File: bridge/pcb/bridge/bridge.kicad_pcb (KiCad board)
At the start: 2 copper layers, 161 x 81 mm, 18 parts, among them J1 Screw_Terminal_01x06, J2 Screw_Terminal_01x06, J3 Screw_Terminal_01x06, J4 Conn_01x23, Q1 PMOS, Q2 PMOS, Q3 PMOS, Q4 PMOS, Q5 PMOS, SW1 SW_SPST, U1 YAAJ_BluePill, U2 J104D2C12VDC.20S

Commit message: Fixed issues, added DAC
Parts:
- added D2: GREEN, LED_THT:LED_D5.0mm, F.Cu at (97.5, 114.8)
- added D3: GREEN, LED_THT:LED_D5.0mm, F.Cu at (104.5, 114.8)
- added D4: GREEN, LED_THT:LED_D5.0mm, F.Cu at (118.5, 114.8)
- added D5: GREEN, LED_THT:LED_D5.0mm, F.Cu at (111.5, 114.8)
- added R10: 1k5, Resistor_THT:R_Axial_DIN0309_L9.0mm_D3.2mm_P12.70mm_Horizontal, F.Cu at (117.8, 63.2)
- added R6: 24k, Resistor_THT:R_Axial_DIN0309_L9.0mm_D3.2mm_P12.70mm_Horizontal, F.Cu at (98.8, 89.8)
- added R7: 24k, Resistor_THT:R_Axial_DIN0309_L9.0mm_D3.2mm_P12.70mm_Horizontal, F.Cu at (104.2, 89.9)
- added R8: 10k, Resistor_THT:R_Axial_DIN0309_L9.0mm_D3.2mm_P12.70mm_Horizontal, F.Cu at (116.5, 89.9)
- added R9: 144k, Resistor_THT:R_Axial_DIN0309_L9.0mm_D3.2mm_P12.70mm_Horizontal, F.Cu at (109.8, 89.9)
- added U3: AD557JN, bridge:AD557JN, F.Cu at (100.0, 65.2)
- Q1, Q2, Q3, Q4, Q5: footprint Package_TO_SOT_THT:TO-3P-3_Horizontal_TabDown -> Package_TO_SOT_THT:TO-220-3_Horizontal_TabDown
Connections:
- U1 pad 25: unconnected-(U1-PA0-Pad25) -> Net-(U1-PA0)
- U1 pad 26: unconnected-(U1-PA1-Pad26) -> Net-(U1-PA1)
- U1 pad 27: unconnected-(U1-PA2-Pad27) -> Net-(U1-PA2)
- U1 pad 28: unconnected-(U1-PA3-Pad28) -> Net-(U1-PA3)
- U1 pad 29: unconnected-(U1-PA4-Pad29) -> Net-(U1-PA4)
- U1 pad 30: unconnected-(U1-PA5-Pad30) -> Net-(U1-PA5)
- U1 pad 31: unconnected-(U1-PA6-Pad31) -> Net-(U1-PA6)
- U1 pad 32: unconnected-(U1-PA7-Pad32) -> Net-(U1-PA7)
- U2 pad 4: ACCEL_AUX_AUTO -> unconnected-(U2-Pad4)
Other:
- board size 161 x 81 mm -> 163 x 83 mm

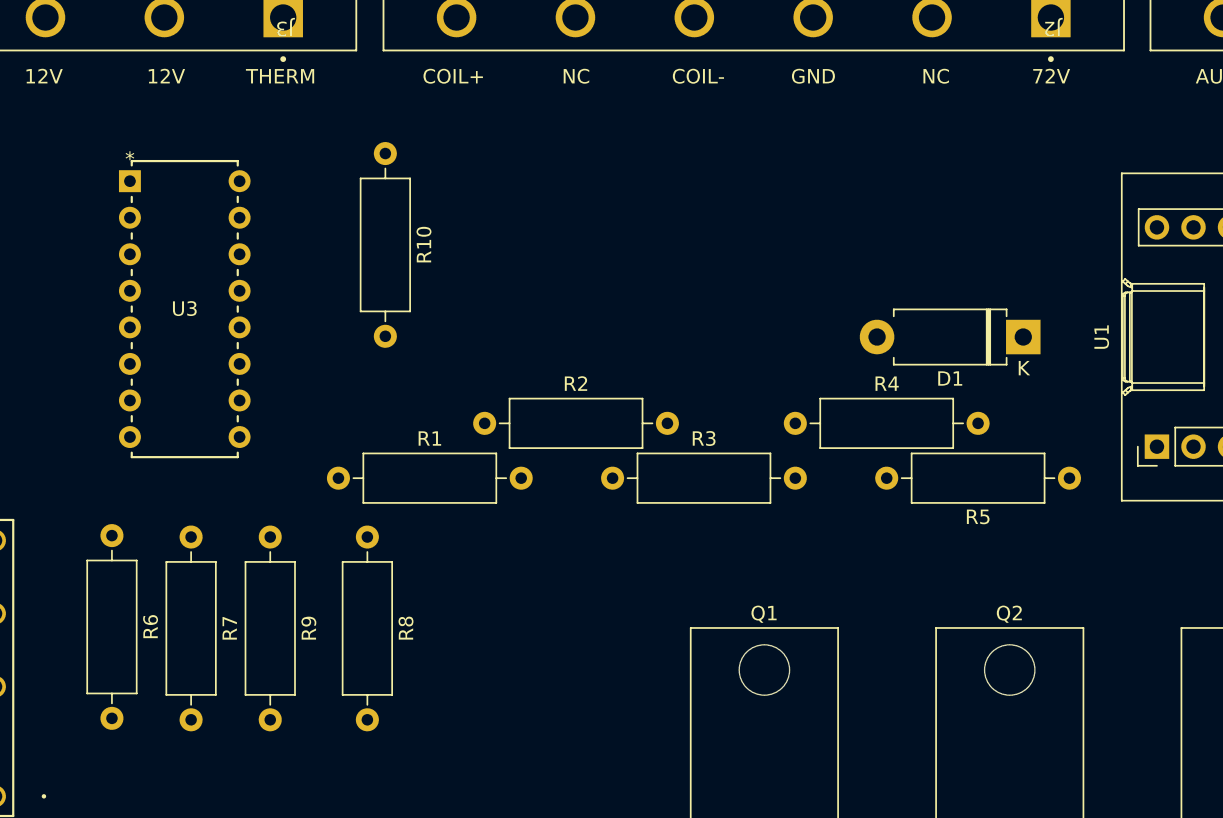
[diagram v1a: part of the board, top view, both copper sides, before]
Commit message: Changed PCB to use correct tht resistor footprint
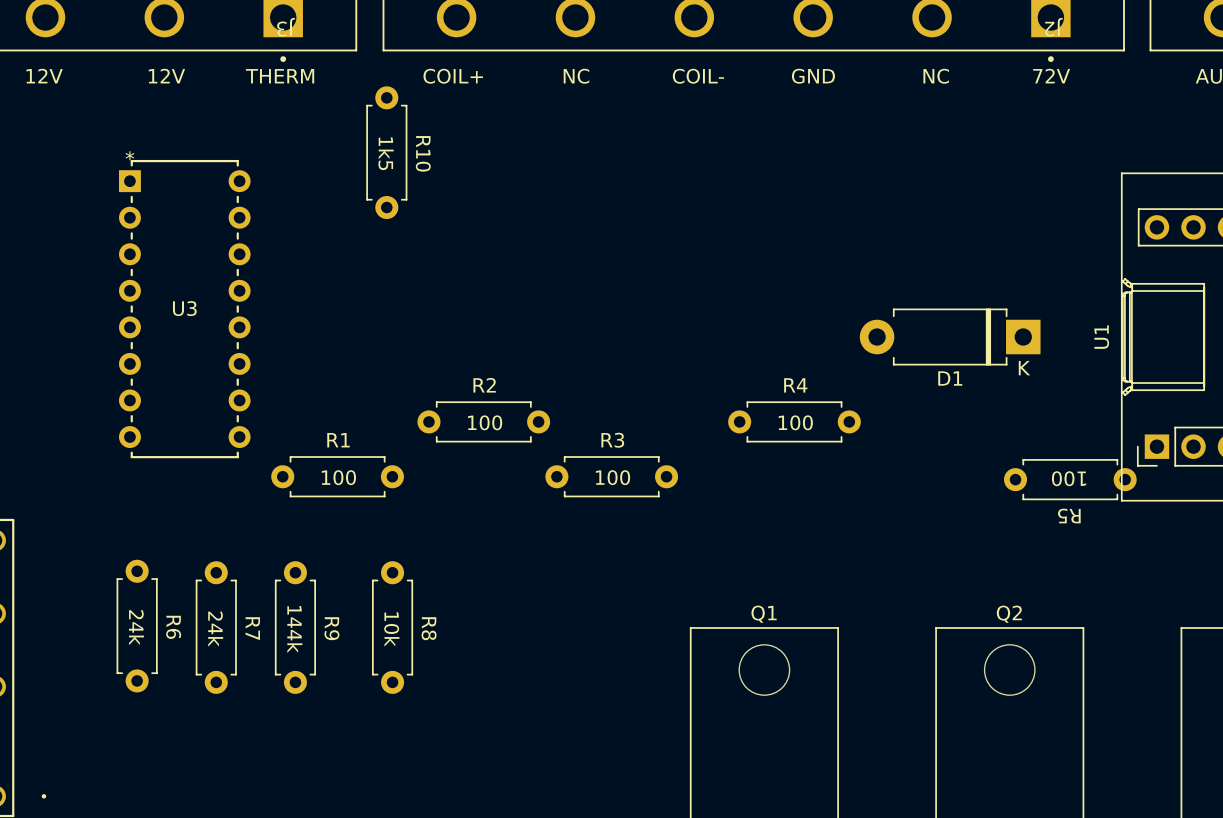
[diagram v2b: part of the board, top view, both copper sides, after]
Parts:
- R1, R10, R2, R3, R4, R5, R6, R7, R8, R9: footprint Resistor_THT:R_Axial_DIN0309_L9.0mm_D3.2mm_P12.70mm_Horizontal -> bridge:THT_RESISTOR_WITH_VALUE
- moved R6 6.56 mm to (100.4, 96.2)
- moved R7 6.56 mm to (105.9, 96.2)
- moved R8 6.56 mm to (118.2, 96.2)
- moved R9 6.56 mm to (111.4, 96.2)

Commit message: Completed schematic
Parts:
- added R11: 47k, bridge:THT_RESISTOR_WITH_VALUE, F.Cu at (129.2, 92.0)
- added R12: 100k, bridge:THT_RESISTOR_WITH_VALUE, F.Cu at (129.2, 96.1)
- moved R5 6.63 mm to (158.8, 86.9)
- moved R10 1.75 mm to (117.8, 65.0)
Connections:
- U1 pad 11: unconnected-(U1-PB3-Pad11) -> MAN_AUTO_STATE
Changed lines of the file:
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@@
   (net 49 "unconnected-(U1-PA12-Pad9)")
   (net 50 "unconnected-(U1-PA15-Pad10)")
-  (net 51 "unconnected-(U1-PB3-Pad11)")
+  (net 51 "MAN_AUTO_STATE")
   (net 52 "unconnected-(U1-3V3-Pad20)")
   (net 53 "unconnected-(U1-VBat-Pad21)")
@@
     )
   )
+  (footprint "bridge:THT_RESISTOR_WITH_VALUE" (layer "F.Cu")
+    (at 129.25 96.1)
+    (property "Sheetfile" "bridge.kicad_sch")
+    (property "Sheetname" "")
+    (property "ki_description" "Resistor")
+    (property "ki_keywords" "R res resistor")
+    (attr through_hole)
+    (fp_text reference "R12" (at 0 -2.6 unlocked) (layer "F.SilkS")
+        (effects (font (size 1 1) (thickness 0.1)))
+    )
+    (fp_text value "100k" (at 0 0 unlocked) (layer "F.SilkS")
+        (effects (font (size 1 1) (thickness 0.15)))
+    )
+    (fp_text user "${REFERENCE}" (at 0 2.5 unlocked) (layer "F.Fab")
+        (effects (font (size 1 1) (thickness 0.15)))
+    )
+    (fp_line (start -3.33 -1.47) (end 3.21 -1.47)
+      (stroke (width 0.12) (type solid)) (layer "F.SilkS"))
+    (fp_line (start -3.33 -1.14) (end -3.33 -1.47)
+      (stroke (width 0.12) (type solid)) (layer "F.SilkS"))
+    (fp_line (start -3.33 0.94) (end -3.33 1.27)
+      (stroke (width 0.12) (type solid)) (layer "F.SilkS"))
+    (fp_line (start -3.33 1.27) (end 3.21 1.27)
+      (stroke (width 0.12) (type solid)) (layer "F.SilkS"))
+    (fp_line (start 3.21 -1.47) (end 3.21 -1.14)
+      (stroke (width 0.12) (type solid)) (layer "F.SilkS"))
+    (fp_line (start 3.21 1.27) (end 3.21 0.94)
+      (stroke (width 0.12) (type solid)) (layer "F.SilkS"))
+    (fp_line (start -4.92 -1.6) (end -4.92 1.4)
+      (stroke (width 0.05) (type solid)) (layer "F.CrtYd"))
+    (fp_line (start -4.92 1.4) (end 4.8 1.4)
+      (stroke (width 0.05) (type solid)) (layer "F.CrtYd"))
+    (fp_line (start 4.8 -1.6) (end -4.92 -1.6)
+      (stroke (width 0.05) (type solid)) (layer "F.CrtYd"))
+    (fp_line (start 4.8 1.4) (end 4.8 -1.6)
+      (stroke (width 0.05) (type solid)) (layer "F.CrtYd"))
+    (fp_line (start -3.87 -0.1) (end -3.21 -0.1)
+      (stroke (width 0.1) (type solid)) (layer "F.Fab"))
+    (fp_line (start -3.21 -1.35) (end -3.21 1.15)
+      (stroke (width 0.1) (type solid)) (layer "F.Fab"))
+    (fp_line (start -3.21 1.15) (end 3.09 1.15)
+      (stroke (width 0.1) (type solid)) (layer "F.Fab"))
+    (fp_line (start 3.09 -1.35) (end -3.21 -1.35)
+      (stroke (width 0.1) (type solid)) (layer "F.Fab"))
+    (fp_line (start 3.09 1.15) (end 3.09 -1.35)
+      (stroke (width 0.1) (type solid)) (layer "F.Fab"))
+    (fp_line (start 3.75 -0.1) (end 3.09 -0.1)
+      (stroke (width 0.1) (type solid)) (layer "F.Fab"))
+    (pad "1" thru_hole circle (at -3.87 -0.1) (size 1.6 1.6) (drill 0.8) (layers "*.Cu" "*.Mask")
+      (net 51 "MAN_AUTO_STATE") (pintype "passive"))
+    (pad "2" thru_hole oval (at 3.75 -0.1) (size 1.6 1.6) (drill 0.8) (layers "*.Cu" "*.Mask")
+      (net 73 "Net-(SW1-A)") (pintype "passive"))
+    (model "${KICAD6_3DMODEL_DIR}/Resistor_THT.3dshapes/R_Axial_DIN0207_L6.3mm_D2.5mm_P7.62mm_Horizontal.wrl"
+      (offset (xyz -4 0 0))
+      (scale (xyz 1 1 1))
+      (rotate (xyz 0 0 0))
+    )
+  )
   (footprint "Package_TO_SOT_THT:TO-220-3_Horizontal_TabDown" (layer "F.Cu")
     (at 141.55 115.8)
@@
   )
   (footprint "bridge:THT_RESISTOR_WITH_VALUE" (layer "F.Cu")
-    (at 165.29 85.81 180)
+    (at 158.75 86.9 180)
     (property "Sheetfile" "mcu.kicad_sch")
     (property "Sheetname" "MCU")
@@
   )
   (footprint "bridge:THT_RESISTOR_WITH_VALUE" (layer "F.Cu")
-    (at 117.75 63.25 -90)
+    (at 117.75 65 -90)
     (property "Sheetfile" "mcu.kicad_sch")
     (property "Sheetname" "MCU")
@@
   )
   (footprint "bridge:THT_RESISTOR_WITH_VALUE" (layer "F.Cu")
+    (at 129.25 92.05)
+    (property "Sheetfile" "bridge.kicad_sch")
+    (property "Sheetname" "")
+    (property "ki_description" "Resistor")
+    (property "ki_keywords" "R res resistor")
+    (attr through_hole)
+    (fp_text reference "R11" (at 0 -2.6 unlocked) (layer "F.SilkS")
+        (effects (font (size 1 1) (thickness 0.1)))
+    )
+    (fp_text value "47k" (at 0 0 unlocked) (layer "F.SilkS")
+        (effects (font (size 1 1) (thickness 0.15)))
+    )
+    (fp_text user "${REFERENCE}" (at 0 2.5 unlocked) (layer "F.Fab")
+        (effects (font (size 1 1) (thickness 0.15)))
+    )
+    (fp_line (start -3.33 -1.47) (end 3.21 -1.47)
+      (stroke (width 0.12) (type solid)) (layer "F.SilkS"))
+    (fp_line (start -3.33 -1.14) (end -3.33 -1.47)
+      (stroke (width 0.12) (type solid)) (layer "F.SilkS"))
+    (fp_line (start -3.33 0.94) (end -3.33 1.27)
+      (stroke (width 0.12) (type solid)) (layer "F.SilkS"))
+    (fp_line (start -3.33 1.27) (end 3.21 1.27)
+      (stroke (width 0.12) (type solid)) (layer "F.SilkS"))
+    (fp_line (start 3.21 -1.47) (end 3.21 -1.14)
+      (stroke (width 0.12) (type solid)) (layer "F.SilkS"))
+    (fp_line (start 3.21 1.27) (end 3.21 0.94)
+      (stroke (width 0.12) (type solid)) (layer "F.SilkS"))
+    (fp_line (start -4.92 -1.6) (end -4.92 1.4)
+      (stroke (width 0.05) (type solid)) (layer "F.CrtYd"))
+    (fp_line (start -4.92 1.4) (end 4.8 1.4)
+      (stroke (width 0.05) (type solid)) (layer "F.CrtYd"))
+    (fp_line (start 4.8 -1.6) (end -4.92 -1.6)
+      (stroke (width 0.05) (type solid)) (layer "F.CrtYd"))
+    (fp_line (start 4.8 1.4) (end 4.8 -1.6)
+      (stroke (width 0.05) (type solid)) (layer "F.CrtYd"))
+    (fp_line (start -3.87 -0.1) (end -3.21 -0.1)
+      (stroke (width 0.1) (type solid)) (layer "F.Fab"))
+    (fp_line (start -3.21 -1.35) (end -3.21 1.15)
+      (stroke (width 0.1) (type solid)) (layer "F.Fab"))
+    (fp_line (start -3.21 1.15) (end 3.09 1.15)
+      (stroke (width 0.1) (type solid)) (layer "F.Fab"))
+    (fp_line (start 3.09 -1.35) (end -3.21 -1.35)
+      (stroke (width 0.1) (type solid)) (layer "F.Fab"))
+    (fp_line (start 3.09 1.15) (end 3.09 -1.35)
+      (stroke (width 0.1) (type solid)) (layer "F.Fab"))
+    (fp_line (start 3.75 -0.1) (end 3.09 -0.1)
+      (stroke (width 0.1) (type solid)) (layer "F.Fab"))
+    (pad "1" thru_hole circle (at -3.87 -0.1) (size 1.6 1.6) (drill 0.8) (layers "*.Cu" "*.Mask")
+      (net 5 "GND") (pintype "passive"))
+    (pad "2" thru_hole oval (at 3.75 -0.1) (size 1.6 1.6) (drill 0.8) (layers "*.Cu" "*.Mask")
+      (net 51 "MAN_AUTO_STATE") (pintype "passive"))
+    (model "${KICAD6_3DMODEL_DIR}/Resistor_THT.3dshapes/R_Axial_DIN0207_L6.3mm_D2.5mm_P7.62mm_Horizontal.wrl"
+      (offset (xyz -4 0 0))
+      (scale (xyz 1 1 1))
+      (rotate (xyz 0 0 0))
+    )
+  )
+  (footprint "bridge:THT_RESISTOR_WITH_VALUE" (layer "F.Cu")
     (at 146.24 82)
     (property "Sheetfile" "mcu.kicad_sch")
@@
       (net 50 "unconnected-(U1-PA15-Pad10)") (pinfunction "PA15") (pintype "bidirectional+no_connect"))
     (pad "11" thru_hole circle (at 0 25.4 90) (size 1.7 1.7) (drill 1) (layers "*.Cu" "*.Mask")
-      (net 51 "unconnected-(U1-PB3-Pad11)") (pinfunction "PB3") (pintype "bidirectional+no_connect"))
+      (net 51 "MAN_AUTO_STATE") (pinfunction "PB3") (pintype "bidirectional"))
     (pad "12" thru_hole circle (at 0 27.94 90) (size 1.7 1.7) (drill 1) (layers "*.Cu" "*.Mask")
       (net 4 "START_SWITCH_NEG_MAN") (pinfunction "PB4") (pintype "bidirectional"))

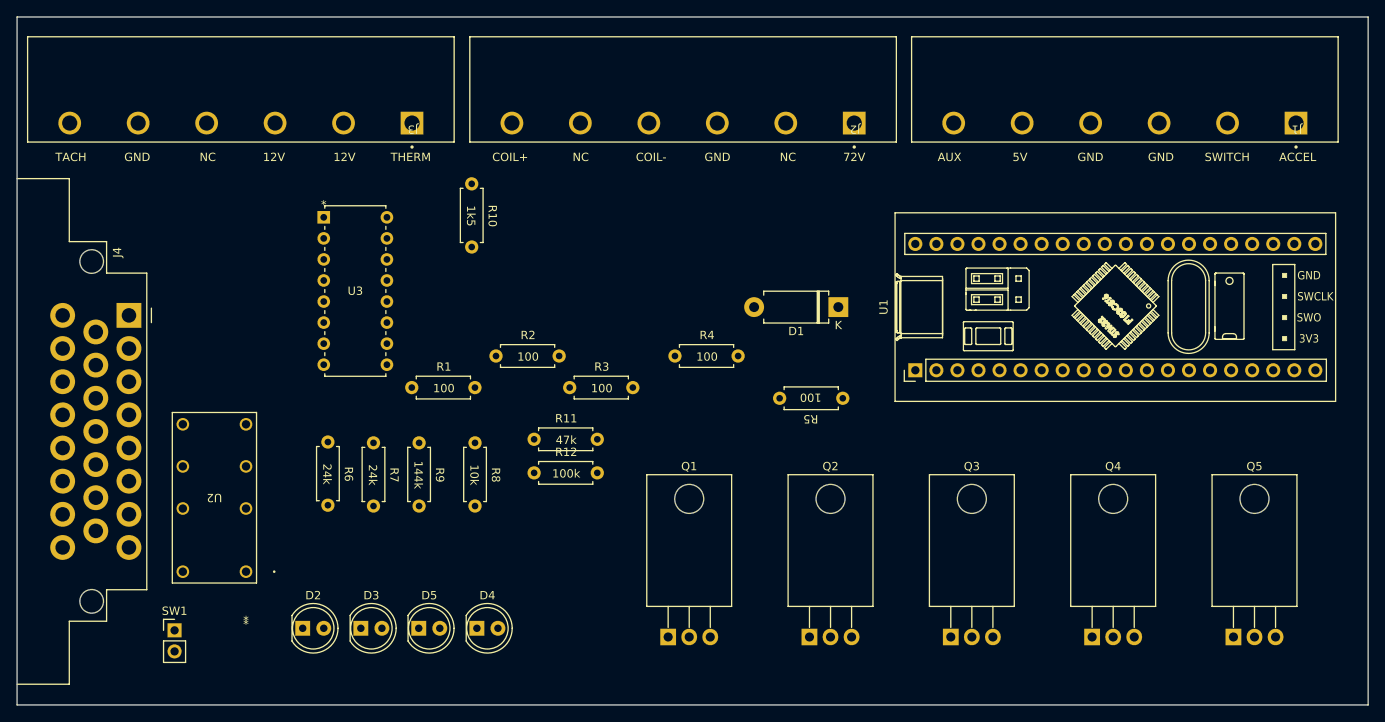
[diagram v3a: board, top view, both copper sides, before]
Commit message: Completed routing of PCB
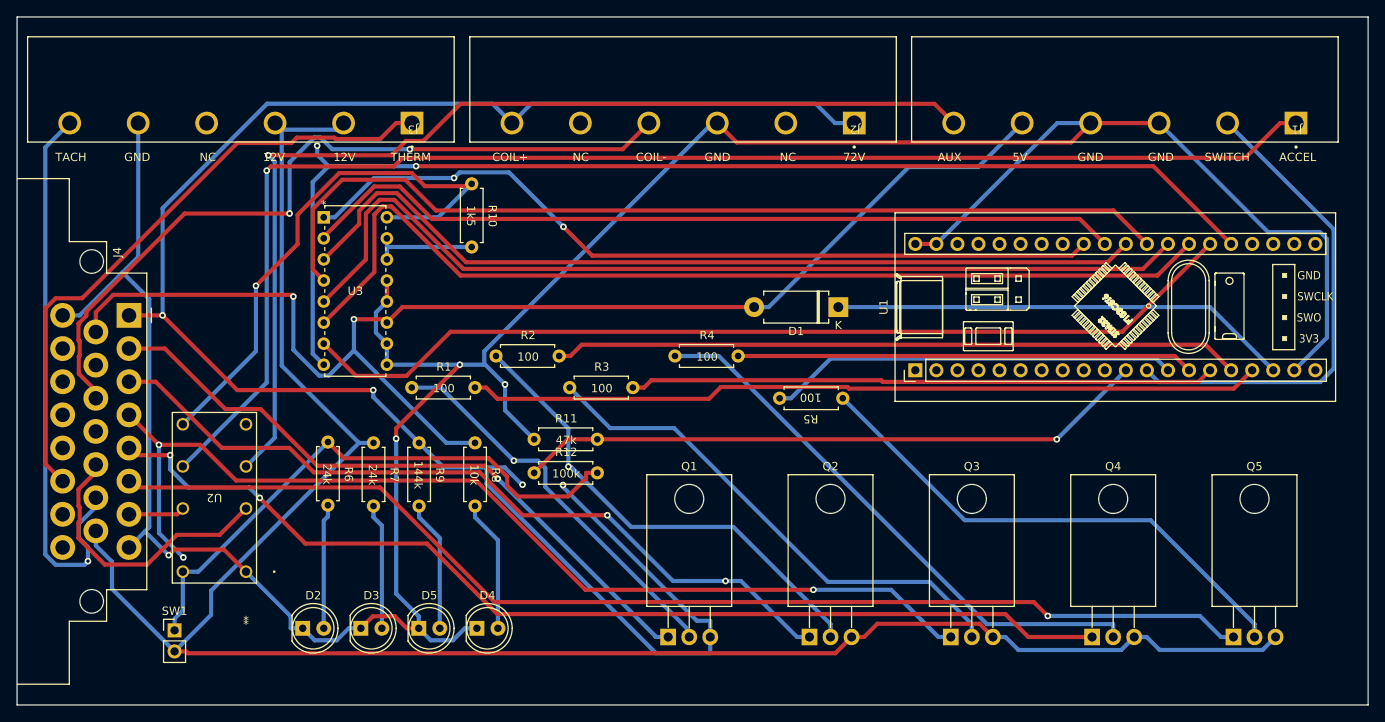
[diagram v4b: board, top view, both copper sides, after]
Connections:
- J2 pad 6: COIL_CONTROL_72V -> +BATT
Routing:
- net GND: track 0.00 -> 351.4 mm, vias 0 -> 4
- net +12V: track 0.00 -> 242.8 mm
- net +BATT: track 0.00 -> 226.9 mm, vias 0 -> 4
- net ACCEL_MAN: track 0.00 -> 166.4 mm, vias 0 -> 1
- net +5V: track 0.00 -> 157.2 mm, vias 0 -> 2
- net Net-(U1-PA0): track 0.00 -> 141.1 mm, vias 0 -> 2
- net TURF_SWITCH: track 0.00 -> 141.0 mm, vias 0 -> 1
- net REVERSE_SWITCH: track 0.00 -> 126.6 mm, vias 0 -> 2
- net ACCEL_AUX_MAN: track 0.00 -> 125.5 mm, vias 0 -> 1
- net FORWARD_SWITCH: track 0.00 -> 125.1 mm, vias 0 -> 3
- net Net-(U1-PA2): track 0.00 -> 119.3 mm
- net Net-(U1-PA1): track 0.00 -> 115.1 mm
- net Net-(U1-PA3): track 0.00 -> 114.9 mm
- net Net-(U1-PA4): track 0.00 -> 114.5 mm
- net Net-(U1-PA5): track 0.00 -> 105.4 mm
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
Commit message: Completed silkscreen
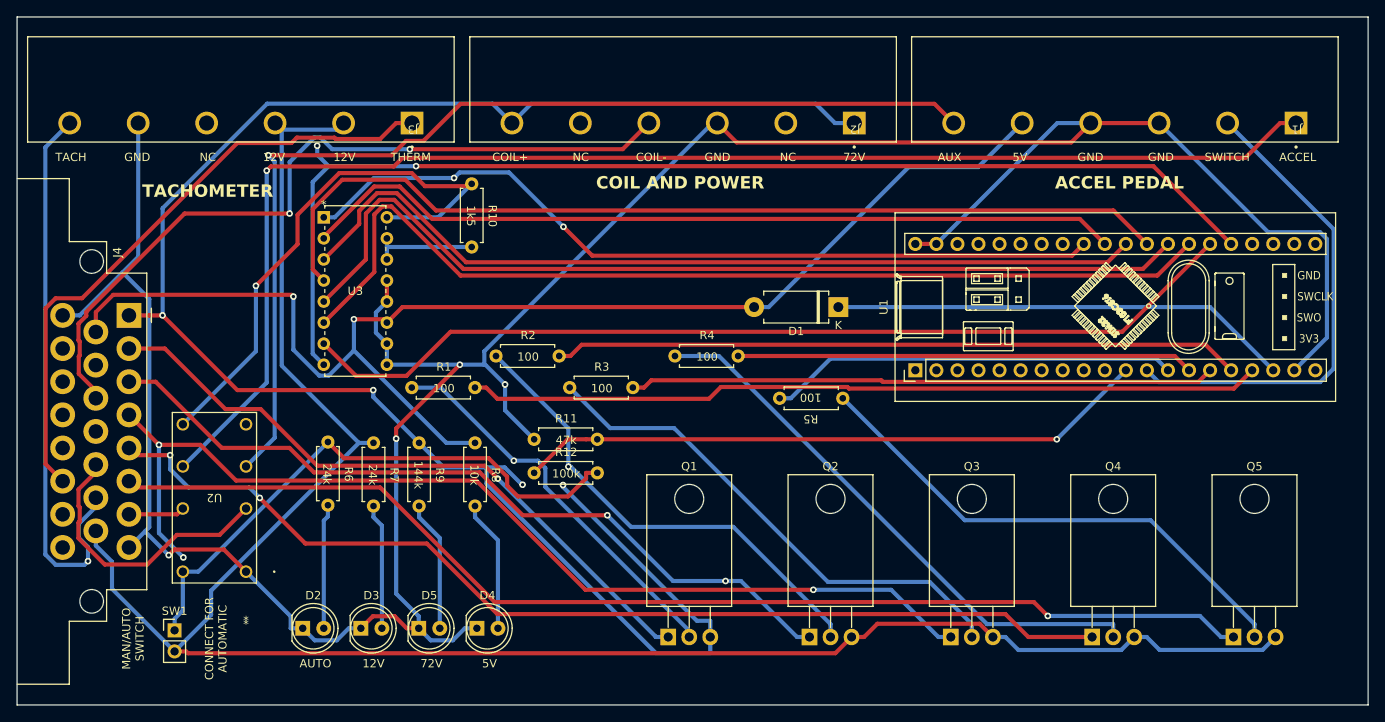
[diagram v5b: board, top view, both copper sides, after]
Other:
- board text added: "ACCEL PEDAL"
- board text added: "AUTO"
- board text added: "COIL AND POWER"
- board text added: "CONNECT FOR AUTOMATIC"
- board text added: "MAN/AUTO SWITCH"
- board text added: "TACHOMETER"
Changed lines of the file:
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@@
     (effects (font (size 1 1) (thickness 0.15)) (justify bottom))
+  )
+  (gr_text "12V" (at 106 119) (layer "F.SilkS")
+    (effects (font (size 1 1) (thickness 0.15)))
+  )
+  (gr_text "MAN/AUTO\nSWITCH" (at 77 116 90) (layer "F.SilkS")
+    (effects (font (size 1 1) (thickness 0.15)))
   )
   (gr_text "5V" (at 184 58.5) (layer "F.SilkS")
     (effects (font (size 1 1) (thickness 0.15)) (justify bottom))
+  )
+  (gr_text "TACHOMETER" (at 86 62) (layer "F.SilkS")
+    (effects (font (size 1.5 1.5) (thickness 0.3) bold))
   )
   (gr_text "12V" (at 102.5 58.5) (layer "F.SilkS")
@@
   (gr_text "GND" (at 77.5 58.5) (layer "F.SilkS")
     (effects (font (size 1 1) (thickness 0.15)) (justify bottom))
+  )
+  (gr_text "COIL AND POWER" (at 143 61) (layer "F.SilkS")
+    (effects (font (size 1.5 1.5) (thickness 0.3) bold))
+  )
+  (gr_text "72V" (at 113 119) (layer "F.SilkS")
+    (effects (font (size 1 1) (thickness 0.15)))
+  )
+  (gr_text "5V" (at 120 119) (layer "F.SilkS")
+    (effects (font (size 1 1) (thickness 0.15)))
   )
   (gr_text "72V" (at 164 58.5) (layer "F.SilkS")
@@
     (effects (font (size 1 1) (thickness 0.15)) (justify bottom))
   )
+  (gr_text "CONNECT FOR\nAUTOMATIC" (at 87 116 90) (layer "F.SilkS")
+    (effects (font (size 1 1) (thickness 0.15)))
+  )
   (gr_text "SWITCH" (at 209 58.5) (layer "F.SilkS")
     (effects (font (size 1 1) (thickness 0.15)) (justify bottom))
@@
     (effects (font (size 1 1) (thickness 0.15)) (justify bottom))
   )
+  (gr_text "AUTO" (at 99 119) (layer "F.SilkS")
+    (effects (font (size 1 1) (thickness 0.15)))
+  )
   (gr_text "GND" (at 201 58.5) (layer "F.SilkS")
     (effects (font (size 1 1) (thickness 0.15)) (justify bottom))
   )
+  (gr_text "ACCEL PEDAL" (at 196 61) (layer "F.SilkS")
+    (effects (font (size 1.5 1.5) (thickness 0.3) bold))
+  )
   (gr_text "AUX" (at 175.5 58.5) (layer "F.SilkS")
